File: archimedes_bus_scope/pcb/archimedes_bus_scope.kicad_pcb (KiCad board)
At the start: 4 copper layers, 149.9 x 99.1 mm, 1 part

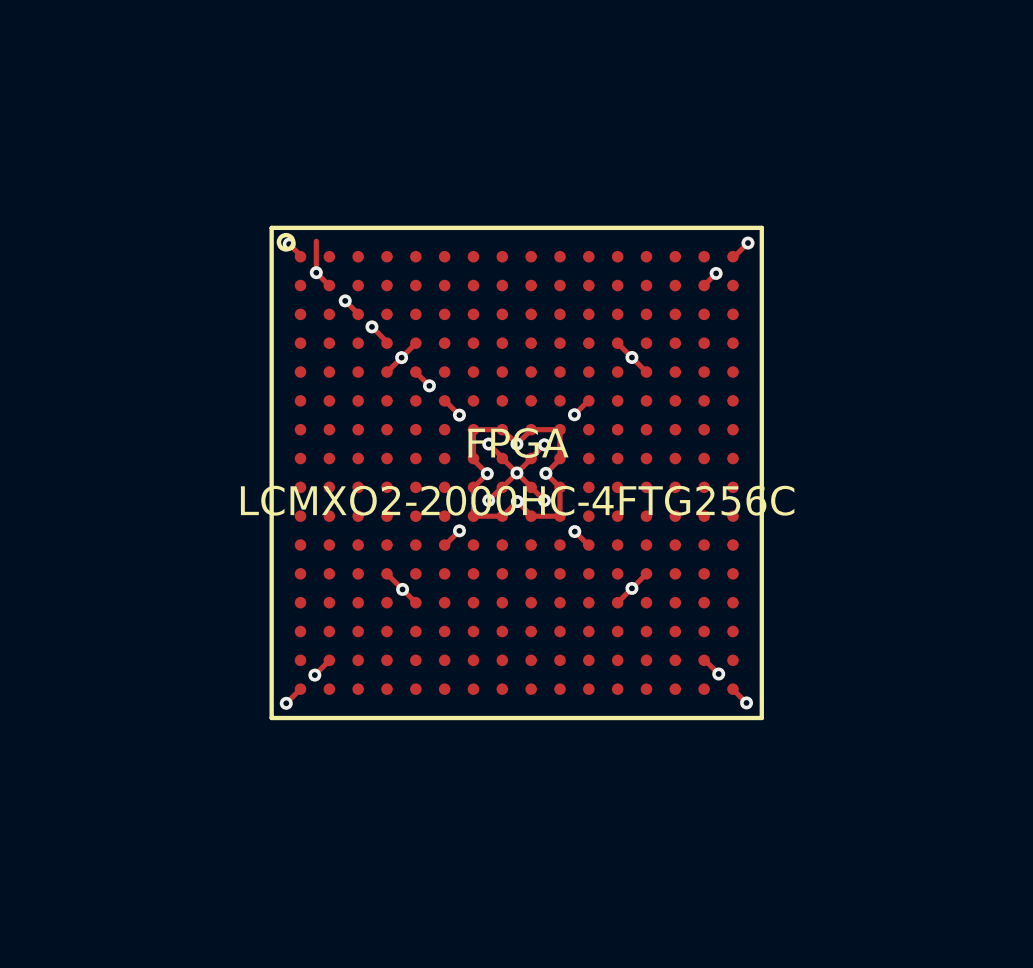
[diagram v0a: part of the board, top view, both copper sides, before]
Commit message: Added some FPGA config signals and got power vias looking good
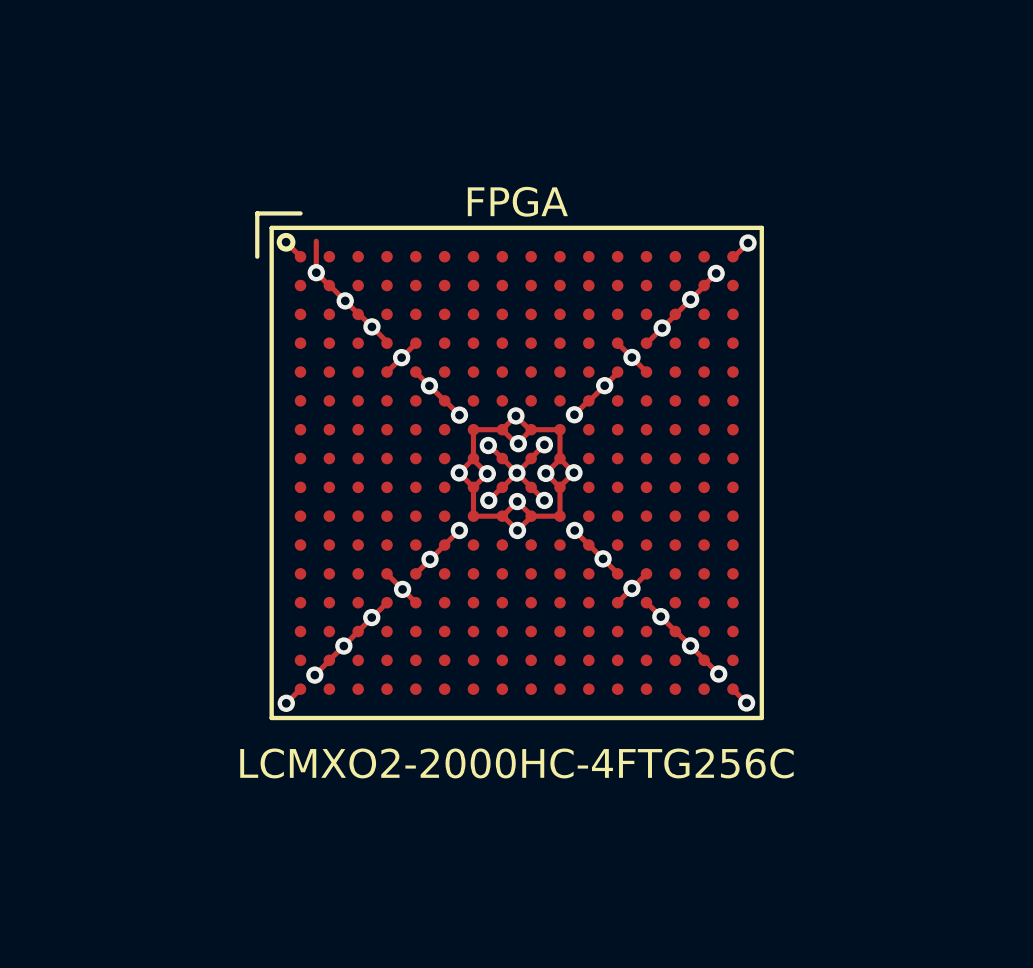
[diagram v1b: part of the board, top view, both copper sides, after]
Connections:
- FPGA pad A13: (no net) -> fpga_INITN
- FPGA pad A2: (no net) -> NC
- FPGA pad A6: (no net) -> fpga_TDI
- FPGA pad A7: (no net) -> fpga_TCK
- FPGA pad B10: (no net) -> fpga_PROGRAMN
- FPGA pad B8: (no net) -> fpga_TMS
- FPGA pad C13: (no net) -> fpga_DONE
- FPGA pad C6: (no net) -> fpga_TDO
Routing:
- net GND: track 14.2 -> 29.2 mm, vias 16 -> 25
- net 3V3: track 22.0 -> 27.8 mm, vias 12 -> 16

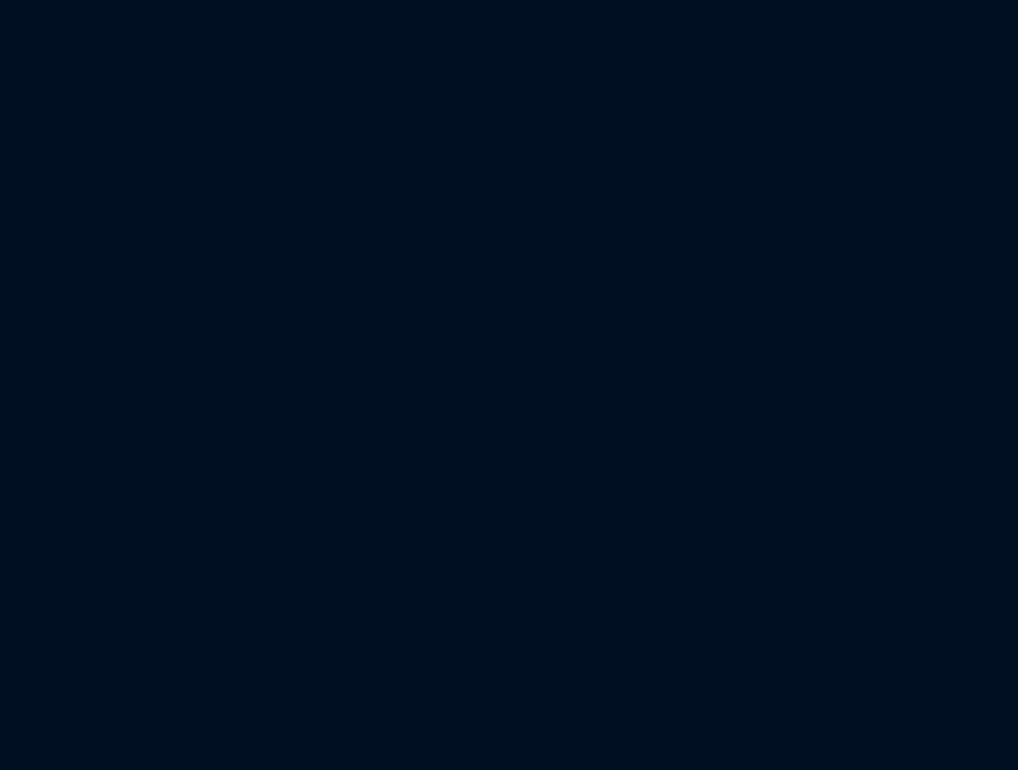
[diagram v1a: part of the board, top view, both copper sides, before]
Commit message: Added JTAG connector for MachXO2 chip
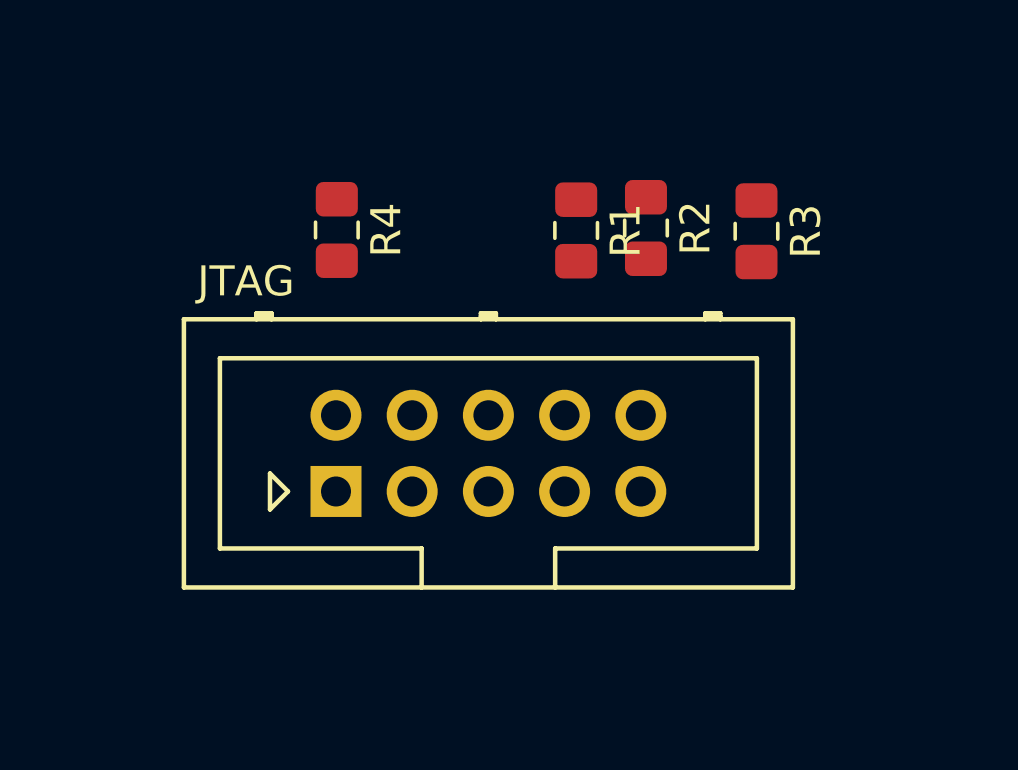
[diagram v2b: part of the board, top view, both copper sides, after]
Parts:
- added JTAG: jtag, Connector_Multicomp:Multicomp_MC9A12-1034_2x05_P2.54mm_Vertical, F.Cu at (168.7, 42.7)
- added R1: 10k, Resistor_SMD:R_0805_2012Metric_Pad1.15x1.40mm_HandSolder, F.Cu at (176.7, 34.0)
- added R2: 10k, Resistor_SMD:R_0805_2012Metric_Pad1.15x1.40mm_HandSolder, F.Cu at (179.0, 34.0)
- added R3: 10k, Resistor_SMD:R_0805_2012Metric_Pad1.15x1.40mm_HandSolder, F.Cu at (182.7, 34.1)
- added R4: 4k7, Resistor_SMD:R_0805_2012Metric_Pad1.15x1.40mm_HandSolder, F.Cu at (168.7, 34.0)
